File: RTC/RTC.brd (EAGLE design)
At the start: 25.4 x 25.4 mm, 8 parts, among them IC1 DS3231/SO

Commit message: Latest version of schematics and boards
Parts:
- removed IC1: DS3231/SO, adafruit:SO16W
- removed LED: blue, led:CHIPLED_1206
- removed U$3: TINY841, IntegerLabs:SOIC14
- added BAT1: 20mm coincell, SparkFun-Electromechanical:BATTCON_20MM_4LEGS
- added C3: (no value), SparkFun-Capacitors:0805
- added C4: .47uF, SparkFun-Capacitors:0805
- added L1: 1mH, SparkFun-Passives:1007
- added LED1: (no value), adafruit:CHIP-LED0805
- added Q2: MC-405, crystal:MC-405
- added R1: 680, SparkFun-Passives:0805
- added R2: 10k, SparkFun-Passives:0805
- added R4: 1, SparkFun-Resistors:0805
- added R5, R6: 2k, SparkFun-Resistors:0805
- added T1: therm, SparkFun-Passives:0805
- added U$1: ATTINY48/88-TQFP, IntegerLabs:TQFP-32
- C1: value 0.1uF -> .47uF
- C2: value 10uF -> 2.2uF; device SparkFun-Capacitors:0805 -> SparkFun-Passives:0805
- R3: value 680 -> 1k
- U$2: value BATTERY -> PCF8523; device IntegerLabs:BU1632 -> IntegerLabs:SOIC-8
- U$4: value FOOTPRINT -> FOOTPRINTFOOTPRINT-2; device IntegerLabs:FOOTPRINT -> IntegerLabs:FOOTPRINT2
- moved R3 27.9 mm to (30.2, 6.03), turned to 0 degrees
- moved C1 15.8 mm to (20.6, 17.8), turned to 270 degrees
- moved C2 14.3 mm to (30.2, 8.57)
- moved U$4 10.2 mm to (35.6, 0.00)
- moved U$2 3.24 mm to (13.3, 9.53), flipped to the top, turned to 0 degrees
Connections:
- removed net DATA: U$3.11
- removed net SCL/SCK: U$3.9, U$4.P$4
- removed net SDA/MOSI: U$3.7, U$4.P$2
- new net AVCC: C4.2, L1.1, R2.1, U$1.18
- new net MOSI: U$1.15, U$4.PROG4
- new net N$7: Q2.1, U$2.1
- new net N$8: Q2.2, U$2.2
- new net RTC_CLKOUT: U$2.7
- new net RTC_SCL: R5.1, U$1.32, U$2.6
- new net RTC_SDA: R6.1, U$1.31, U$2.5
- new net SCK: U$1.17, U$4.PROG2
- new net SCL: U$1.28, U$4.BUS3
- new net SDA: U$1.27, U$4.BUS1
- new net THERM: C3.1, R2.2, T1.2, U$1.25
- net GND: now also BAT1.2, C2.2, C3.2, C4.1, LED1.C, T1.1, U$1.21, U$1.5, U$2.4, U$4.BUS0; no longer C2.1, IC1.13, LED.C, U$2.-, U$3.14, U$4.P$3
- net LED: now also R1.2, U$1.13; no longer R3.2, U$3.12
- net MISO: now also U$1.16, U$4.PROG3; no longer U$3.8, U$4.MISO
- net N$2: now also R4.2, U$4.BUS2; no longer IC1.16, U$3.2
- net N$3: now also C2.1, R3.1, U$2.8; no longer IC1.15, U$3.3
- net N$5: now also LED1.A, R1.1; no longer LED.A, R3.1
- net RESET: now also U$1.29, U$4.PROG1; no longer U$3.4, U$4.RESET
- net VBAT: now also BAT1.1, U$2.3; no longer IC1.14, U$2.+
- net VCC: now also L1.2, R3.2, R4.1, R5.2, R6.2, U$1.4, U$4.PROG0; no longer C2.2, IC1.2, U$3.1, U$4.P$1
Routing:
- net VCC: track 41.5 -> 80.5 mm, vias 0 -> 2
- net SDA: track 0.00 -> 31.0 mm, vias 0 -> 2
- net SDA/MOSI: track 27.2 -> 0.00 mm
- net SCL: track 0.00 -> 26.9 mm, vias 0 -> 2
- net SCL/SCK: track 19.6 -> 0.00 mm
- net VBAT: track 4.51 -> 22.4 mm
- net AVCC: track 0.00 -> 17.7 mm
- net N$2: track 26.1 -> 11.9 mm, vias 2 -> 0
- net SCK: track 0.00 -> 12.2 mm, vias 0 -> 2
- net MISO: track 16.0 -> 5.96 mm, vias 2 -> 0
- net MOSI: track 0.00 -> 9.31 mm
- net THERM: track 0.00 -> 9.14 mm
- net RTC_SCL: track 0.00 -> 8.35 mm
- net RTC_SDA: track 0.00 -> 7.08 mm
- net N$7: track 0.00 -> 5.85 mm
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- added copper zone on layer 16, net GND
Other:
- board size 25.4 x 25.4 mm -> 35.6 x 29.8 mm
- board text added: "Modulo"
- board text added: "Time and Temp"
- board text added: "v3 2014-09-18"
- board text removed: "2014-06-03"
- board text removed: "RTC v1"

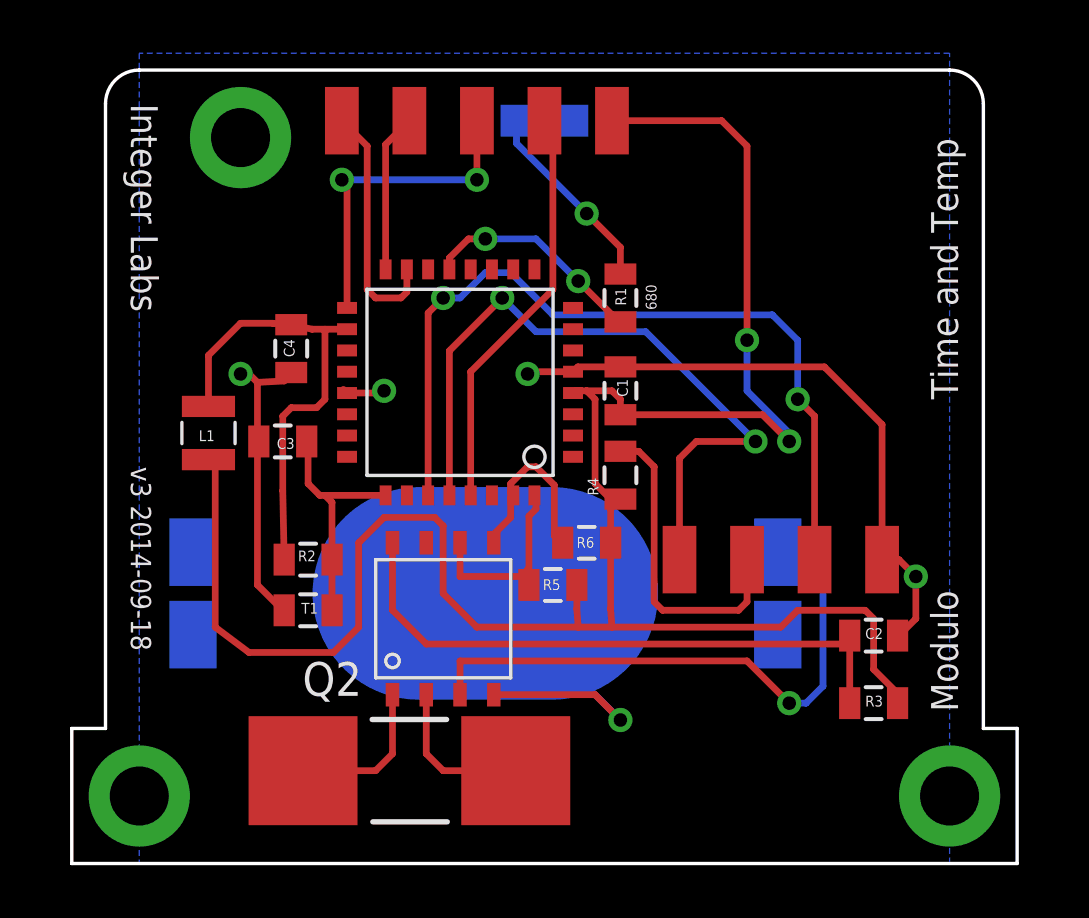
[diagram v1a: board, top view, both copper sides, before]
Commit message: Changed to use attiny841
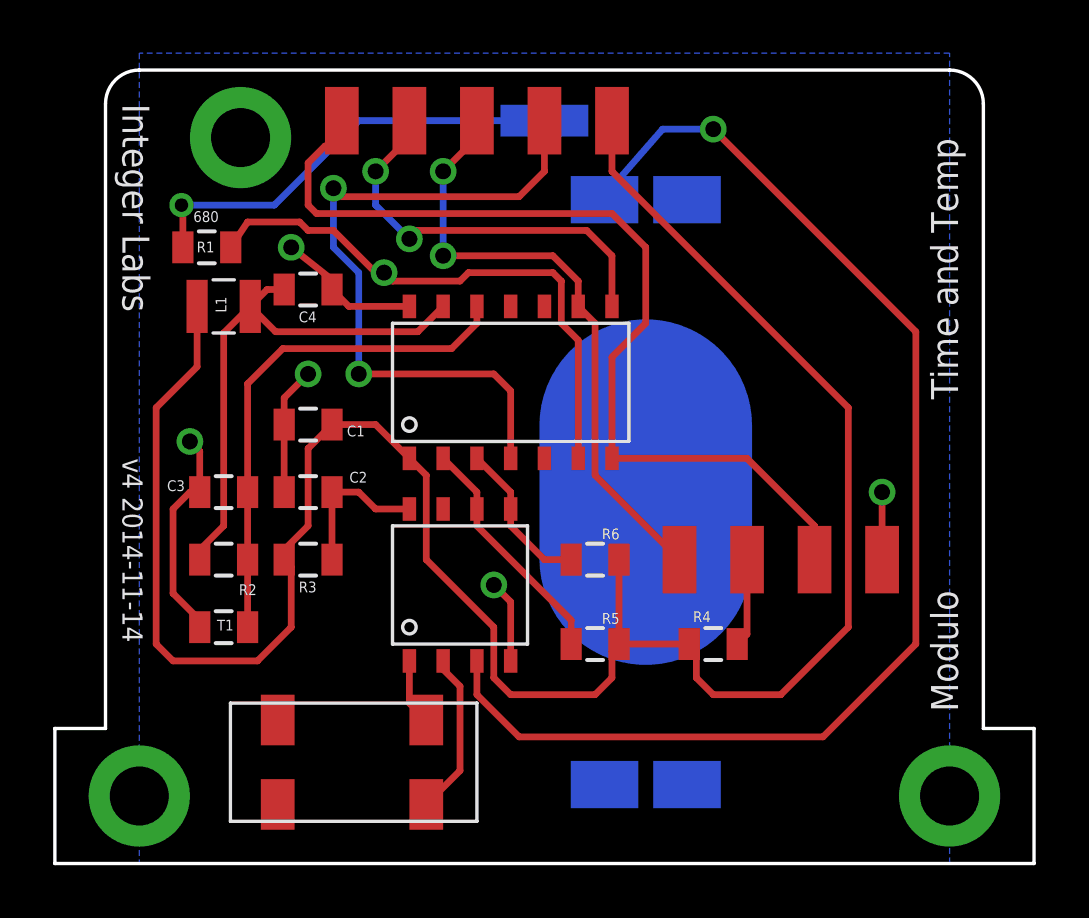
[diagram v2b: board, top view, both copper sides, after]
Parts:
- removed Q2: MC-405, crystal:MC-405
- added U$3: TINY841, IntegerLabs:SOIC14
- C2: value 2.2uF -> 3.3uF
- U$1: value ATTINY48/88-TQFP -> 9HT7-32.768KDZF-T; device IntegerLabs:TQFP-32 -> IntegerLabs:CRYSTAL-ABS25
- moved C2 21.9 mm to (8.89, 14.0), turned to 180 degrees
- moved R3 21.9 mm to (8.89, 11.4), turned to 180 degrees
- moved R1 15.7 mm to (5.08, 23.2), turned to 0 degrees
- moved U$1 12.8 mm to (13.3, 5.40)
- moved C1 11.8 mm to (8.89, 16.5), turned to 0 degrees
- moved R4 7.25 mm to (24.1, 8.26), turned to 0 degrees
- moved BAT1 7.13 mm to (21.6, 14.0), turned to 270 degrees
- moved L1 4.80 mm to (5.71, 21.0), turned to 270 degrees
- moved T1 3.24 mm to (5.71, 8.89)
- moved R2 3.18 mm to (5.71, 11.4)
- moved C3 2.93 mm to (5.71, 14.0)
- moved R5 2.73 mm to (19.7, 8.26)
- moved C4 2.31 mm to (8.89, 21.6), turned to 180 degrees
- moved U$2 1.42 mm to (14.0, 10.8)
- moved R6 0.71 mm to (19.7, 11.4)
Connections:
- removed net MOSI: U$1.15, U$4.PROG4
- removed net N$7: Q2.1, U$2.1
- removed net N$8: Q2.2, U$2.2
- removed net SCK: U$1.17, U$4.PROG2
- removed net SCL: U$1.28, U$4.BUS3
- removed net SDA: U$1.27, U$4.BUS1
- new net N$4: U$1.P$1, U$2.1
- new net N$6: U$1.P$4, U$2.2
- new net SCL/SCK: U$3.9, U$4.BUS3, U$4.PROG2
- new net SDA/MOSI: U$3.7, U$4.BUS1, U$4.PROG4
- net AVCC: now also U$3.13; no longer U$1.18
- net GND: now also U$3.14; no longer U$1.21, U$1.5
- net LED: now also U$3.6; no longer U$1.13
- net MISO: now also U$3.8; no longer U$1.16
- net RESET: now also U$3.4; no longer U$1.29
- net RTC_SCL: now also U$3.2; no longer U$1.32
- net RTC_SDA: now also U$3.3; no longer U$1.31
- net THERM: now also U$3.12; no longer U$1.25
- net VCC: now also U$3.1; no longer U$1.4
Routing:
- net SDA/MOSI: track 0.00 -> 35.7 mm
- net SDA: track 31.0 -> 0.00 mm, vias 2 -> 0
- net SCL: track 26.9 -> 0.00 mm, vias 2 -> 0
- net VBAT: track 22.4 -> 47.8 mm
- net SCL/SCK: track 0.00 -> 23.1 mm, vias 0 -> 2
- net GND: track 49.2 -> 28.0 mm
- net N$3: track 22.8 -> 5.71 mm
- net LED: track 8.45 -> 21.1 mm, vias 2 -> 1
- net SCK: track 12.2 -> 0.00 mm, vias 2 -> 0
- net RESET: track 15.5 -> 26.5 mm, vias 0 -> 2
- net THERM: track 9.14 -> 19.4 mm
- net MISO: track 5.96 -> 15.5 mm, vias 0 -> 2
- net MOSI: track 9.31 -> 0.00 mm
- net N$2: track 11.9 -> 3.33 mm
- net N$5: track 7.39 -> 15.5 mm
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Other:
- board size 35.6 x 29.8 mm -> 36.8 x 29.8 mm
- board text added: "v4 2014-11-14"
- board text removed: "v3 2014-09-18"

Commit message: Switched to attiny841 and made the battery insert from the side.
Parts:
- C3: value (none) -> .1uF
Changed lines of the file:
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@@
 <attribute name="VALUE" x="6.604" y="8.128" size="0.4064" layer="27" rot="R180"/>
 </element>
-<element name="C3" library="SparkFun-Capacitors" package="0805" value="" x="5.715" y="13.97" smashed="yes" rot="R180">
+<element name="C3" library="SparkFun-Capacitors" package="0805" value=".1uF" x="5.715" y="13.97" smashed="yes" rot="R180">
 <attribute name="NAME" x="4.2545" y="14.4145" size="0.4064" layer="25" rot="R180"/>
 <attribute name="VALUE" x="6.731" y="15.367" size="0.4064" layer="27" rot="R180"/>

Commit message: Checkpointing PCB designs
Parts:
- C2: value 3.3uF -> 10uF
- moved U$4 35.6 mm to (0.00, 0.00), flipped to the top
- moved R1 25.4 mm to (30.5, 23.2), flipped to the bottom
- moved C3 24.1 mm to (29.8, 14.0), flipped to the bottom
- moved L1 24.1 mm to (29.8, 21.0), flipped to the bottom
- moved R2 24.1 mm to (29.8, 11.4), flipped to the bottom
- moved T1 24.1 mm to (29.8, 8.89), flipped to the bottom
- moved C1 17.8 mm to (26.7, 16.5), flipped to the bottom
- moved C2 17.8 mm to (26.7, 14.0), flipped to the bottom
- moved C4 17.8 mm to (26.7, 21.6), flipped to the bottom
- moved R3 17.8 mm to (26.7, 11.4), flipped to the bottom
- moved R4 12.7 mm to (11.4, 8.26), flipped to the bottom
- moved U$3 10.2 mm to (22.9, 18.4), flipped to the bottom
- moved U$1 8.89 mm to (22.2, 5.40), flipped to the bottom
- moved BAT1 7.62 mm to (14.0, 14.0), flipped to the top
- moved U$2 7.62 mm to (21.6, 10.8), flipped to the bottom
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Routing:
- added copper zone on layer 1, net GND
- removed copper zone on layer 16, net GND
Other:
- board size 36.8 x 29.8 mm -> 36.3 x 29.8 mm
- board text removed: "Integer Labs"
- board text removed: "Modulo"
- board text removed: "Time and Temp"
- board text removed: "v4 2014-11-14"
